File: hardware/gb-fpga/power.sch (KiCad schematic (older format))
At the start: 25 parts, among them J3 BAT+, J4 BAT-, SW1 SW_SPST, U4 LTC3555

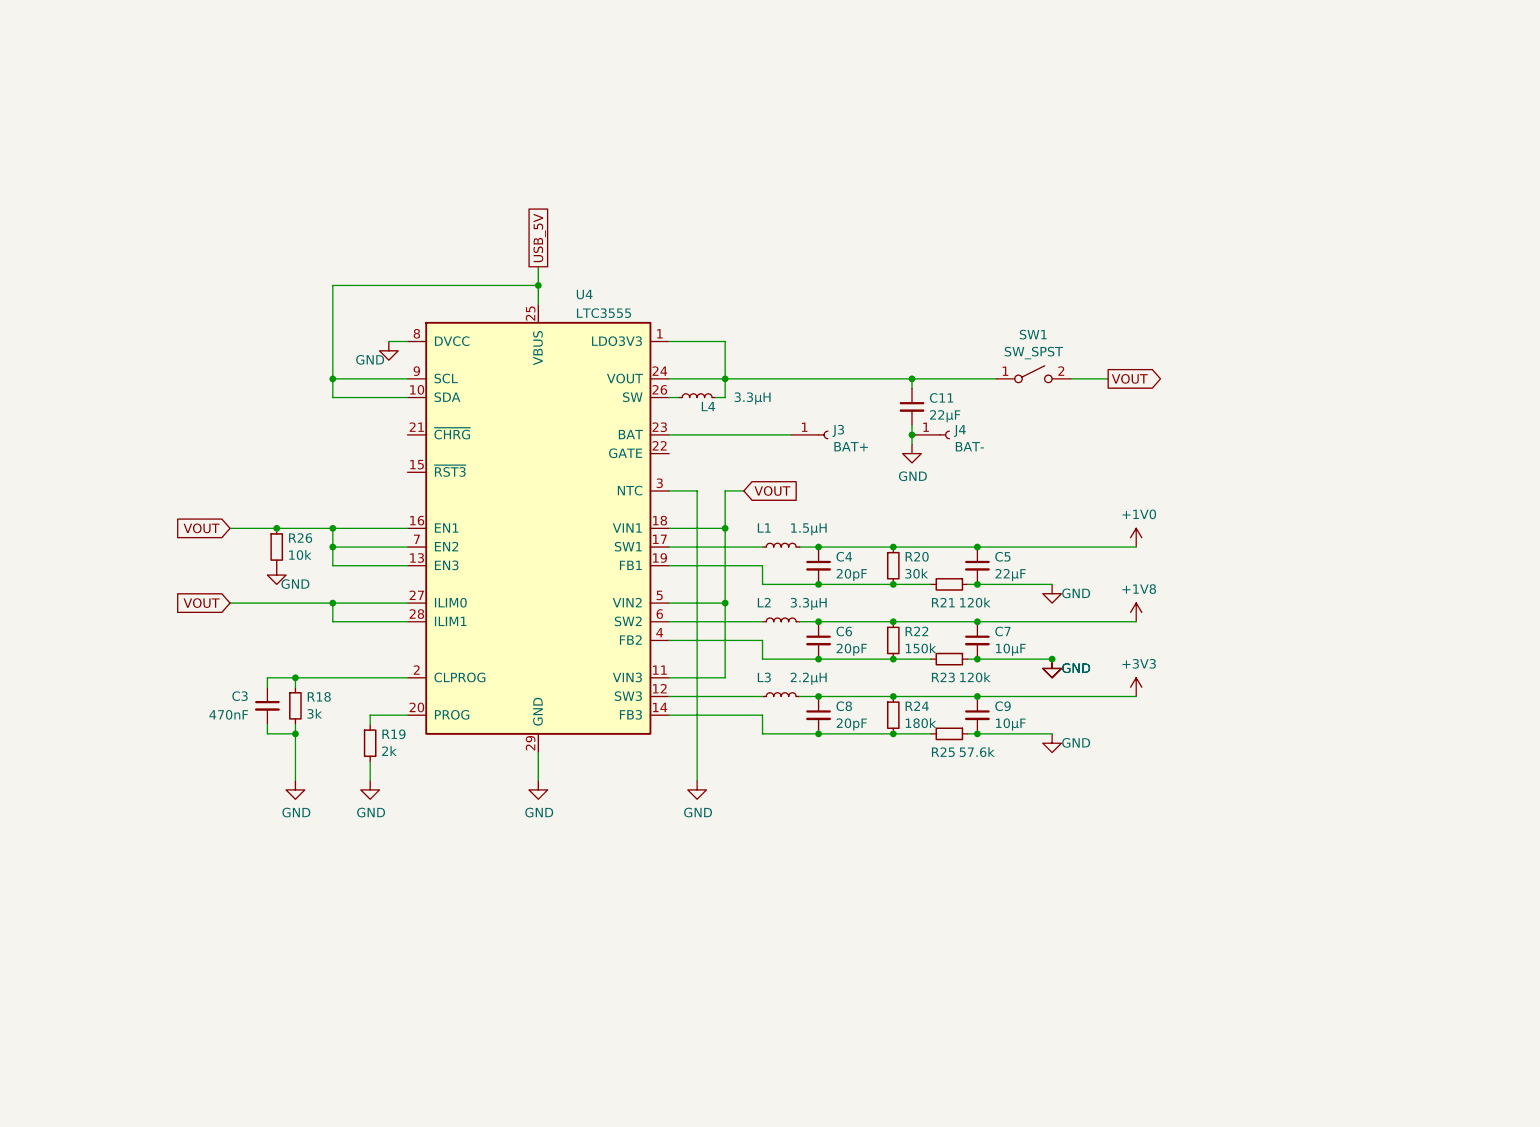
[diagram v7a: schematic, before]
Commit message: Use power up sequence recommended for Spartan FPGA
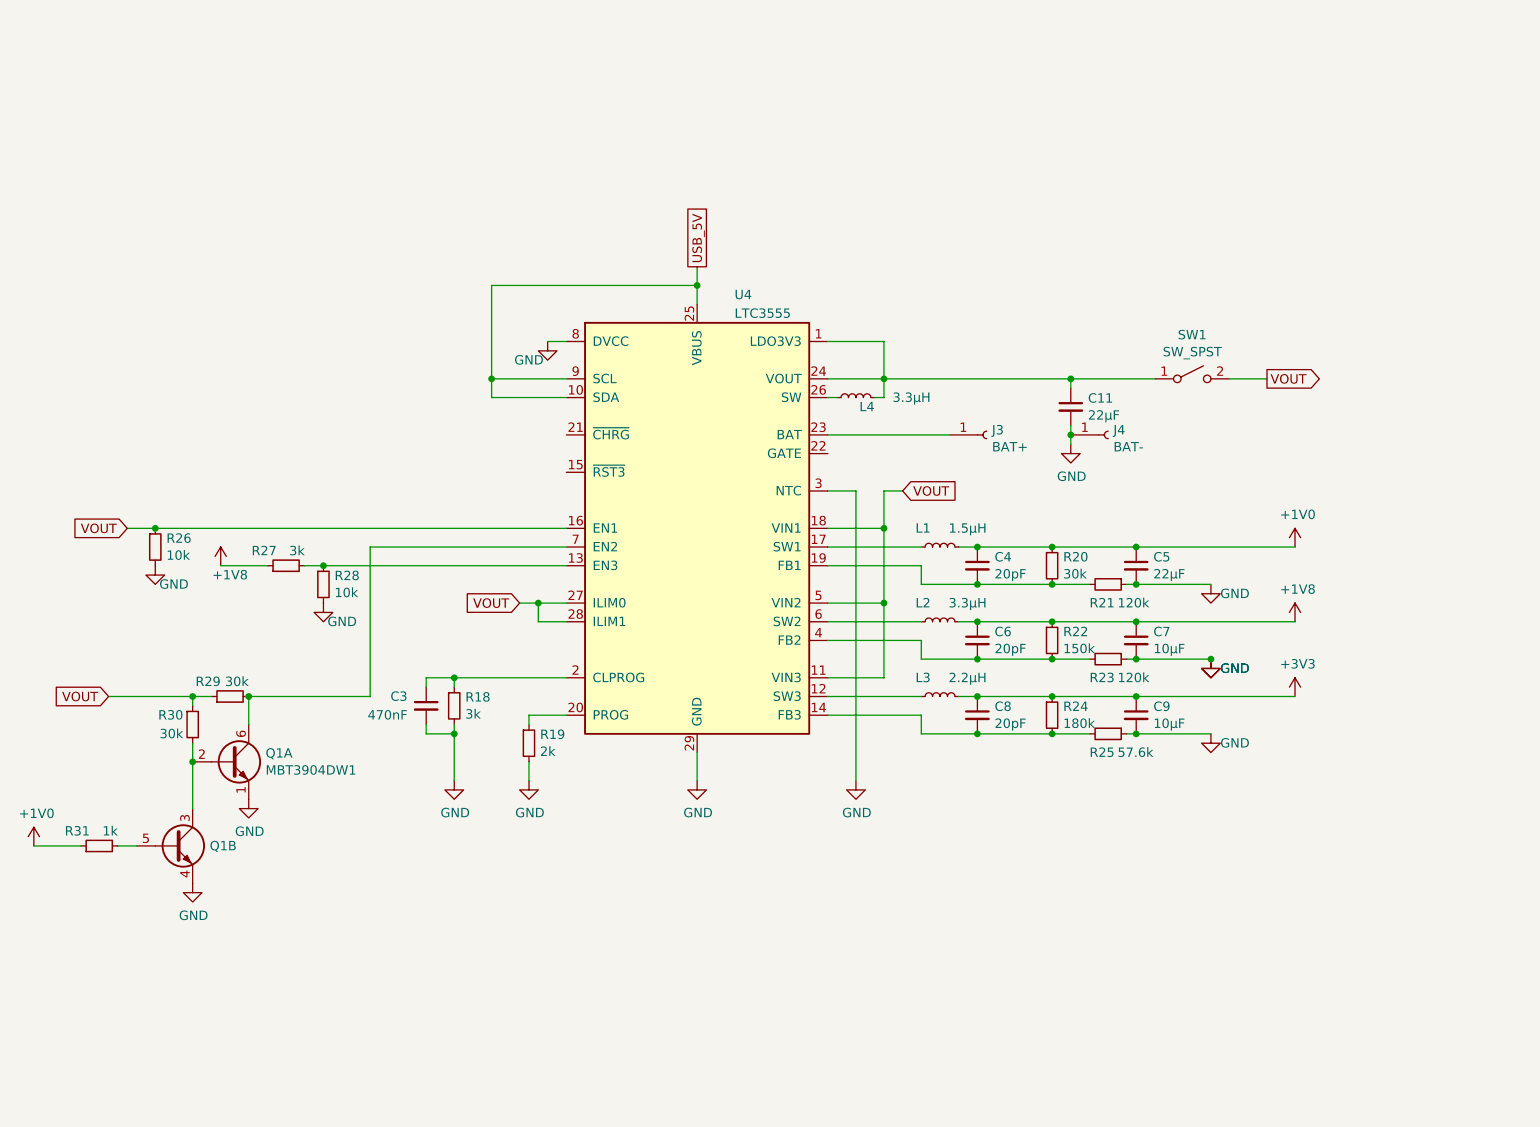
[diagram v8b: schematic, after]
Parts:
- added Q1: MBT3904DW1, Package_TO_SOT_SMD:SOT-363_SC-70-6, symbol Transistor_BJT:MBT3904DW1
- added R27: 3k, Resistor_SMD:R_0603_1608Metric, symbol Device:R_Small
- added R28: 10k, Resistor_SMD:R_0603_1608Metric, symbol Device:R_Small
- added R29, R30: 30k, Resistor_SMD:R_0603_1608Metric, symbol Device:R_Small
- added R31: 1k, Resistor_SMD:R_0603_1608Metric, symbol Device:R_Small
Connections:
- net +1V0: now also R31.1
- net +1V8: now also R27.1
- net GND: now also Q1.1 (E1), Q1.4 (E2), R28.2
- net VOUT: now also R29.1, R30.1; no longer U4.13 (EN3), U4.7 (EN2)
- new net: R27.2, R28.1, U4.13 (EN3)
- new net: Q1.6 (C1), R29.2, U4.7 (EN2)
- new net: Q1.2 (B1), Q1.3 (C2), R30.2
- new net: Q1.5 (B2), R31.2
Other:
- moved on the sheet: C11, C3, C4, C5, C6, C7, C8, C9, J3, J4, L1, L2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
